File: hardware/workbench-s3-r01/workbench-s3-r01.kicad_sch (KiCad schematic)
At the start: 47 parts, among them J1 YD P1 / RIGHT SOCKET / 1x22, J2 DISPLAY HARNESS / 3V3, J4 EXPANSION / 3V3 IO, J5 EXTERNAL BOOT / GPIO0 TO GND, J6 EXTERNAL RESET / EN TO GND, J7 YD P2 / LEFT SOCKET / 1x22, SW1 KEY_1 MX HOTSWAP, SW10 KEY_10 MX HOTSWAP, SW11 KEY_11 MX HOTSWAP, SW12 KEY_12 MX HOTSWAP, SW13 KEY_13 MX HOTSWAP, SW14 KEY_14 MX HOTSWAP, SW15 KEY_15 MX HOTSWAP, SW16 KEY_16 MX HOTSWAP, SW17 KEY_17 MX HOTSWAP, SW18 KEY_18 MX HOTSWAP, SW2 KEY_2 MX HOTSWAP, SW3 KEY_3 MX HOTSWAP, SW4 KEY_4 MX HOTSWAP, SW5 KEY_5 MX HOTSWAP, SW6 KEY_6 MX HOTSWAP, SW7 KEY_7 MX HOTSWAP, SW8 KEY_8 MX HOTSWAP, SW9 KEY_9 MX HOTSWAP

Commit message: Update application workflows and supporting components
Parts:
- added J8: LOWER / IDC20 TO J9 / 1:1, Connector_IDC:IDC-Header_2x10_P2.54mm_Vertical, symbol Connector_Generic:Conn_02x10_Odd_Even
- added J9: UPPER / IDC20 TO J8 / 1:1, Connector_IDC:IDC-Header_2x10_P2.54mm_Vertical, symbol Connector_Generic:Conn_02x10_Odd_Even
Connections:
- net +3V3: now also J8.2 (Pin_2), J8.20 (Pin_20); no longer C1.1, C2.1, J2.2 (Pin_2), R1.1, R2.1
- net GND: now also J8.1 (Pin_1), J8.12 (Pin_12); no longer C1.2, C2.2, J2.1 (Pin_1)
- net GPIO10: now also J8.9 (Pin_9); no longer SW10.1, SW16.1, SW4.1
- net GPIO11: now also J8.10 (Pin_10); no longer SW11.1, SW17.1, SW5.1
- net GPIO12: now also J8.11 (Pin_11); no longer SW12.1, SW18.1, SW6.1
- net GPIO13: now also J8.13 (Pin_13); no longer J2.4 (Pin_4), R1.2
- net GPIO14: now also J8.14 (Pin_14); no longer J2.3 (Pin_3), R2.2
- net GPIO15: now also J8.15 (Pin_15); no longer J2.5 (Pin_5)
- net GPIO16: now also J8.16 (Pin_16); no longer J2.6 (Pin_6)
- net GPIO17: now also J8.17 (Pin_17); no longer J2.7 (Pin_7)
- net GPIO18: now also J8.18 (Pin_18); no longer J2.8 (Pin_8)
- net GPIO21: now also J8.19 (Pin_19); no longer J2.9 (Pin_9)
- net GPIO4: now also J8.3 (Pin_3); no longer D1.1 (K), D2.1 (K), D3.1 (K), D4.1 (K), D5.1 (K), D6.1 (K)
- net GPIO5: now also J8.4 (Pin_4); no longer D10.1 (K), D11.1 (K), D12.1 (K), D7.1 (K), D8.1 (K), D9.1 (K)
- net GPIO6: now also J8.5 (Pin_5); no longer D13.1 (K), D14.1 (K), D15.1 (K), D16.1 (K), D17.1 (K), D18.1 (K)
- net GPIO7: now also J8.6 (Pin_6); no longer SW1.1, SW13.1, SW7.1
- net GPIO8: now also J8.7 (Pin_7); no longer SW14.1, SW2.1, SW8.1
- net GPIO9: now also J8.8 (Pin_8); no longer SW15.1, SW3.1, SW9.1
- net KEY_10_A renamed UP_KEY_10_A
- net KEY_11_A renamed UP_KEY_11_A
- net KEY_12_A renamed UP_KEY_12_A
- net KEY_13_A renamed UP_KEY_13_A
- net KEY_14_A renamed UP_KEY_14_A
- net KEY_15_A renamed UP_KEY_15_A
- net KEY_16_A renamed UP_KEY_16_A
- net KEY_17_A renamed UP_KEY_17_A
- net KEY_18_A renamed UP_KEY_18_A
- net KEY_1_A renamed UP_KEY_1_A
- net KEY_2_A renamed UP_KEY_2_A
- net KEY_3_A renamed UP_KEY_3_A
- net KEY_4_A renamed UP_KEY_4_A
- net KEY_5_A renamed UP_KEY_5_A
- net KEY_6_A renamed UP_KEY_6_A
- net KEY_7_A renamed UP_KEY_7_A
- net KEY_8_A renamed UP_KEY_8_A
- net KEY_9_A renamed UP_KEY_9_A
- new net UP_3V3: C1.1, C2.1, J2.2 (Pin_2), J9.2 (Pin_2), J9.20 (Pin_20), R1.1, R2.1
- new net UP_GND: C1.2, C2.2, J2.1 (Pin_1), J9.1 (Pin_1), J9.12 (Pin_12)
- new net UP_GPIO10: J9.9 (Pin_9), SW10.1, SW16.1, SW4.1
- new net UP_GPIO11: J9.10 (Pin_10), SW11.1, SW17.1, SW5.1
- new net UP_GPIO12: J9.11 (Pin_11), SW12.1, SW18.1, SW6.1
- new net UP_GPIO13: J2.4 (Pin_4), J9.13 (Pin_13), R1.2
- new net UP_GPIO14: J2.3 (Pin_3), J9.14 (Pin_14), R2.2
- new net UP_GPIO15: J2.5 (Pin_5), J9.15 (Pin_15)
- new net UP_GPIO16: J2.6 (Pin_6), J9.16 (Pin_16)
- new net UP_GPIO17: J2.7 (Pin_7), J9.17 (Pin_17)
- new net UP_GPIO18: J2.8 (Pin_8), J9.18 (Pin_18)
- new net UP_GPIO21: J2.9 (Pin_9), J9.19 (Pin_19)
- new net UP_GPIO4: D1.1 (K), D2.1 (K), D3.1 (K), D4.1 (K), D5.1 (K), D6.1 (K), J9.3 (Pin_3)
- new net UP_GPIO5: D10.1 (K), D11.1 (K), D12.1 (K), D7.1 (K), D8.1 (K), D9.1 (K), J9.4 (Pin_4)
- new net UP_GPIO6: D13.1 (K), D14.1 (K), D15.1 (K), D16.1 (K), D17.1 (K), D18.1 (K), J9.5 (Pin_5)
- new net UP_GPIO7: J9.6 (Pin_6), SW1.1, SW13.1, SW7.1
- new net UP_GPIO8: J9.7 (Pin_7), SW14.1, SW2.1, SW8.1
- new net UP_GPIO9: J9.8 (Pin_8), SW15.1, SW3.1, SW9.1
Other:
- note added: "TWO-BOARD REVIEW DRAFT: J8 to J9 uses a pin-1-to-pin-1 IDC20 cable. NO COPPER ACROSS BREAKAWAY TABS."
- note added: "UP_* nets are on the upper board. Lower and upper nets join ONLY through the external cable; see interconnect.csv."
- note removed: "REVIEW DRAFT: PCB placement only; no routing or fabrication release."
- note removed: "YD ESP32-S3 SOCKETED CARRIER. Reuse native USB-C. Firmware display + diode-matrix rollover support pending."

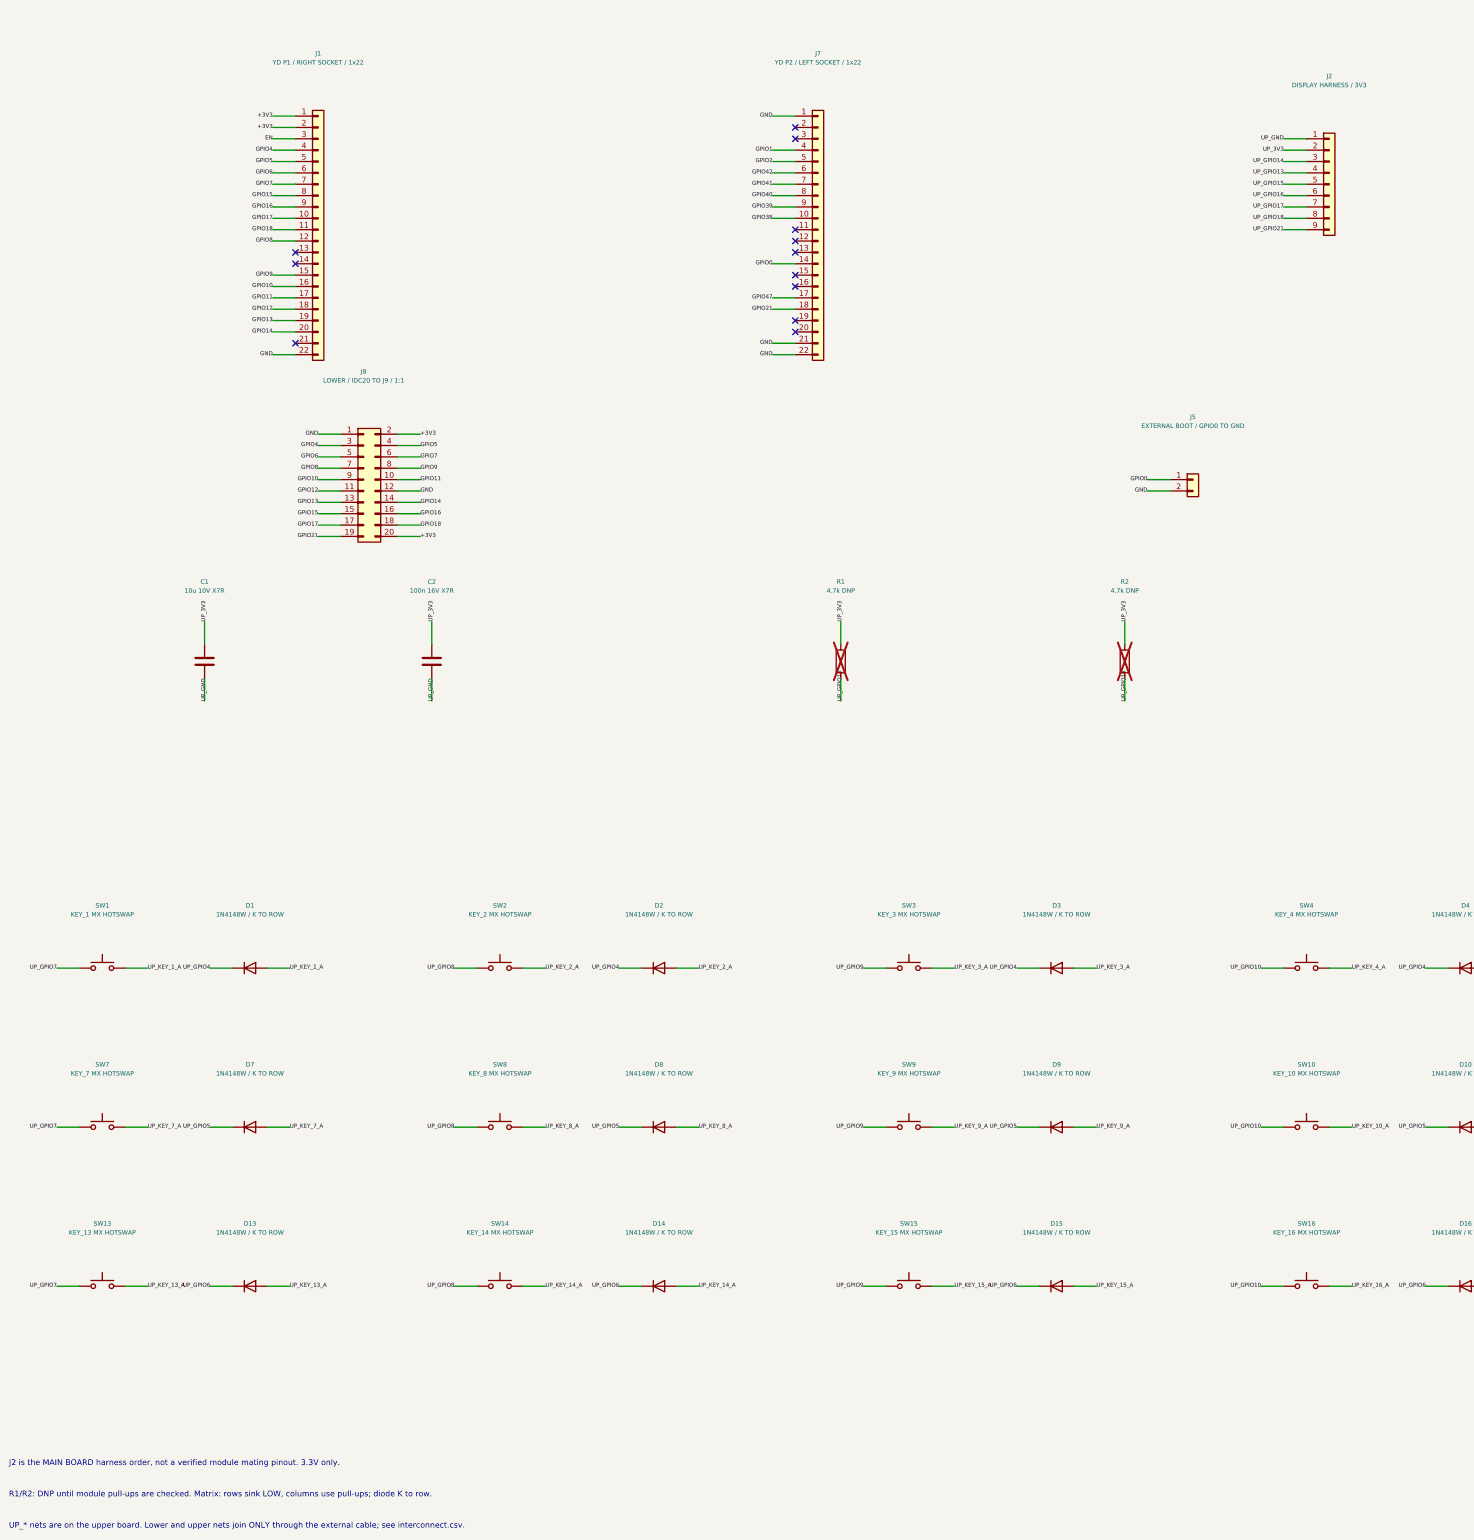
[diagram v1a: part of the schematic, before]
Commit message: fix: correct Workbench S3 display connector and mounting geometry
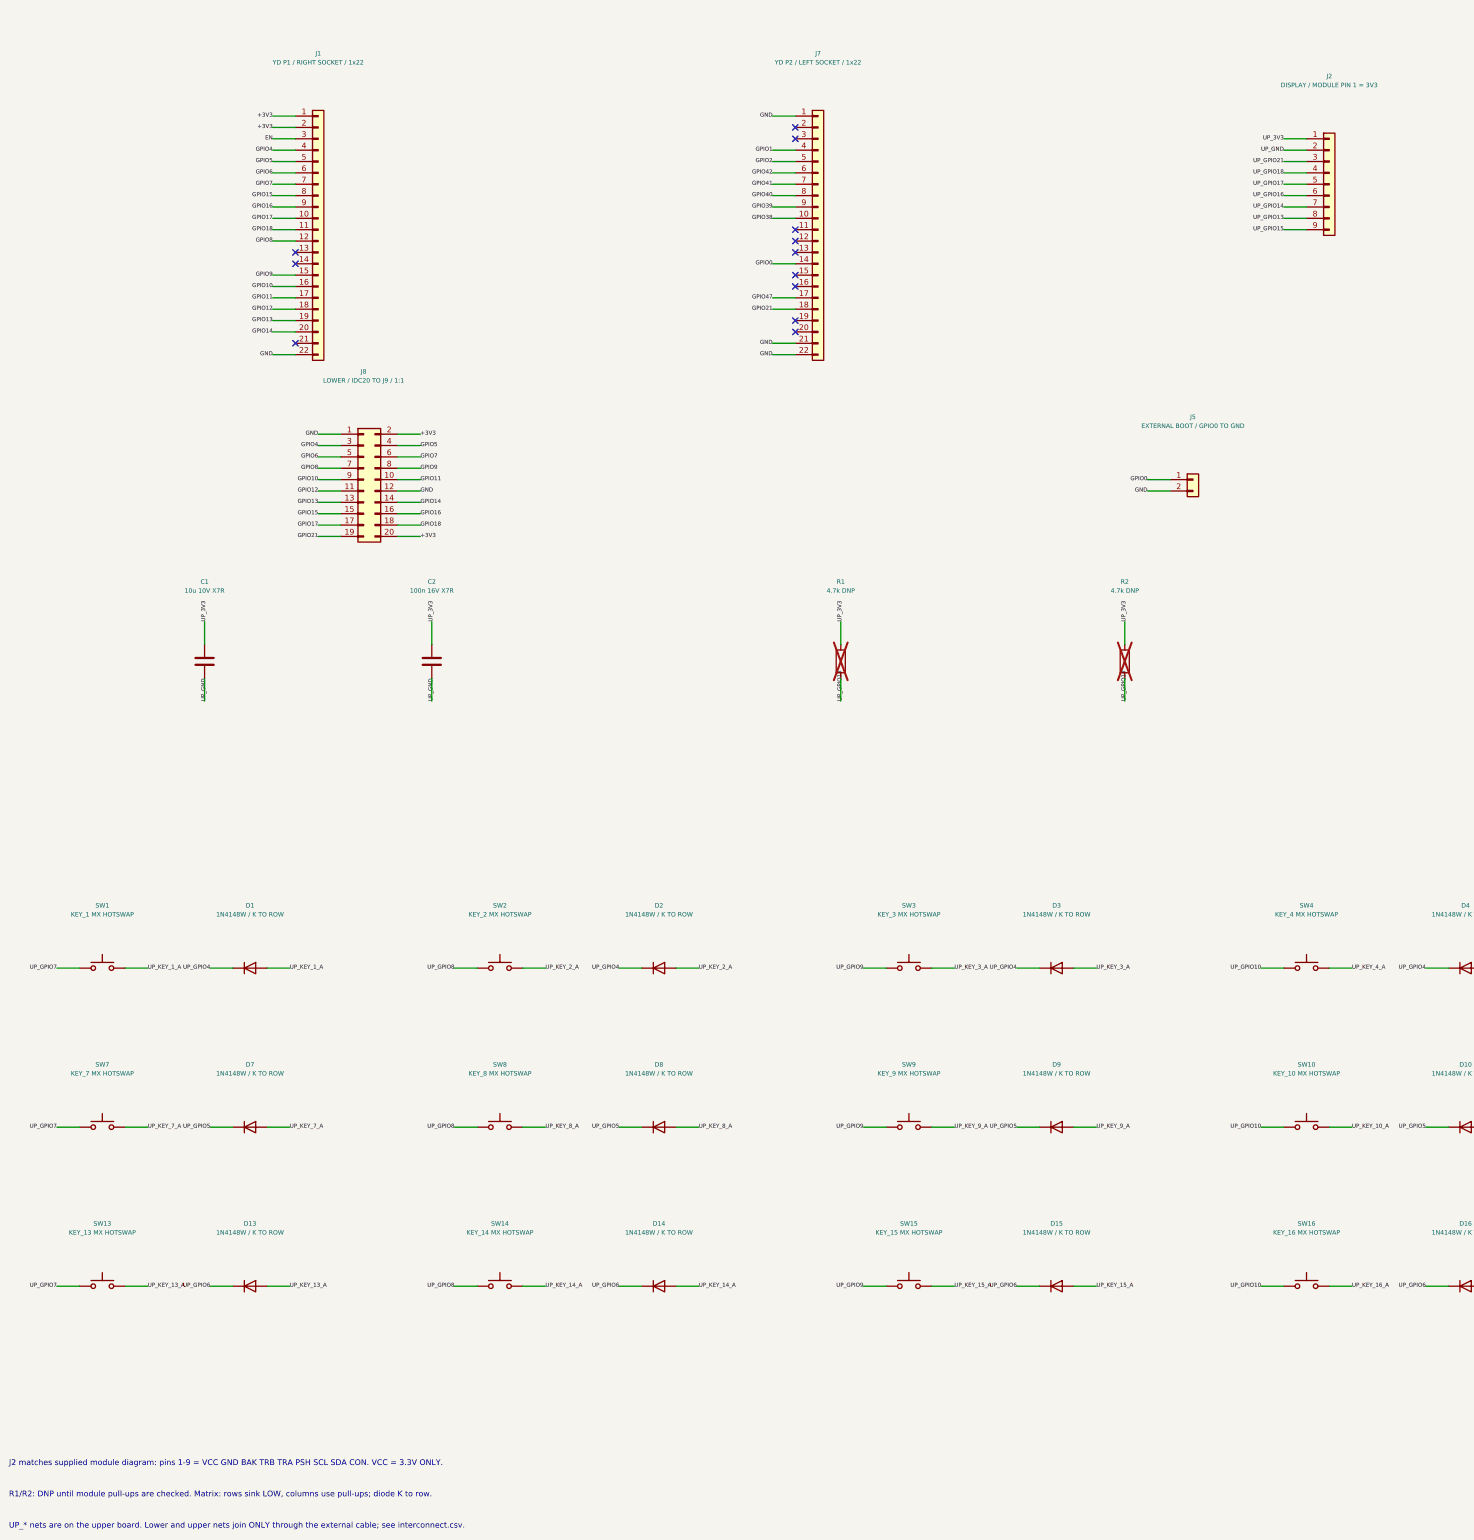
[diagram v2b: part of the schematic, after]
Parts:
- J2: value DISPLAY HARNESS / 3V3 -> DISPLAY / MODULE PIN 1 = 3V3
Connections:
- net UP_3V3: now also J2.1 (Pin_1); no longer J2.2 (Pin_2)
- net UP_GND: now also J2.2 (Pin_2); no longer J2.1 (Pin_1)
- net UP_GPIO13: now also J2.8 (Pin_8); no longer J2.4 (Pin_4)
- net UP_GPIO14: now also J2.7 (Pin_7); no longer J2.3 (Pin_3)
- net UP_GPIO15: now also J2.9 (Pin_9); no longer J2.5 (Pin_5)
- net UP_GPIO17: now also J2.5 (Pin_5); no longer J2.7 (Pin_7)
- net UP_GPIO18: now also J2.4 (Pin_4); no longer J2.8 (Pin_8)
- net UP_GPIO21: now also J2.3 (Pin_3); no longer J2.9 (Pin_9)
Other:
- note added: "J2 matches supplied module diagram: pins 1-9 = VCC GND BAK TRB TRA PSH SCL SDA CON. VCC = 3.3V ONLY."
- note removed: "J2 is the MAIN BOARD harness order, not a verified module mating pinout. 3.3V only."
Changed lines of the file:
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@@
       )
     )
-    (property "Value" "DISPLAY HARNESS / 3V3"
+    (property "Value" "DISPLAY / MODULE PIN 1 = 3V3"
       (at 330.2 71.82000000000001 0)
       (effects
@@
     )
   )
-  (label "UP_GND"
+  (label "UP_3V3"
     (at 320.04 83.82 0)
     (effects
@@
     )
   )
-  (label "UP_3V3"
+  (label "UP_GND"
     (at 320.04 86.36 0)
     (effects
@@
     )
   )
-  (label "UP_GPIO14"
+  (label "UP_GPIO21"
     (at 320.04 88.9 0)
     (effects
@@
     )
   )
-  (label "UP_GPIO13"
+  (label "UP_GPIO18"
     (at 320.04 91.44 0)
     (effects
@@
     )
   )
-  (label "UP_GPIO15"
+  (label "UP_GPIO17"
     (at 320.04 93.98 0)
     (effects
@@
     )
   )
-  (label "UP_GPIO17"
+  (label "UP_GPIO14"
     (at 320.04 99.06 0)
     (effects
@@
     )
   )
-  (label "UP_GPIO18"
+  (label "UP_GPIO13"
     (at 320.04 101.6 0)
     (effects
@@
     )
   )
-  (label "UP_GPIO21"
+  (label "UP_GPIO15"
     (at 320.04 104.14 0)
     (effects
@@
     )
   )
-  (text "J2 is the MAIN BOARD harness order, not a verified module mating pinout. 3.3V only."
+  (text "J2 matches supplied module diagram: pins 1-9 = VCC GND BAK TRB TRA PSH SCL SDA CON. VCC = 3.3V ONLY."
     (at 35 380 0)
     (effects

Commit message: Update application implementation and supporting files
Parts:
- added C3: 100n 16V X7R / U1, Capacitor_SMD:C_0805_2012Metric_Pad1.18x1.45mm_HandSolder, symbol Device:C
- added R4: 10k U1 RESET PULLUP, Resistor_SMD:R_0805_2012Metric_Pad1.20x1.40mm_HandSolder, symbol Device:R
- added U1: MCP23017-E/SO / 0x20, Package_SO:SOIC-28W_7.5x17.9mm_P1.27mm, symbol Interface_Expansion:MCP23017x-x-SO
- J4: value EXPANSION / 3V3 IO -> EXPANSION / 22 SPARE GPIO / 3V3 IO; footprint Connector_PinHeader_2.54mm:PinHeader_1x10_P2.54mm_Vertical -> Connector_PinHeader_2.54mm:PinHeader_1x24_P2.54mm_Vertical; symbol Connector_Generic:Conn_01x10 -> Connector_Generic:Conn_01x24
- J8: value LOWER / IDC20 TO J9 / 1:1 -> LOWER / I2C4 TO J9 / 1:1; footprint Connector_IDC:IDC-Header_2x10_P2.54mm_Vertical -> Connector_JST:JST_XH_B4B-XH-A_1x04_P2.50mm_Vertical; symbol Connector_Generic:Conn_02x10_Odd_Even -> Connector_Generic:Conn_01x04
- J9: value UPPER / IDC20 TO J8 / 1:1 -> UPPER / I2C4 TO J8 / 1:1; footprint Connector_IDC:IDC-Header_2x10_P2.54mm_Vertical -> Connector_JST:JST_XH_B4B-XH-A_1x04_P2.50mm_Vertical; symbol Connector_Generic:Conn_02x10_Odd_Even -> Connector_Generic:Conn_01x04
- R1, R2: value 4.7k DNP -> 2.2k I2C PULLUP; now fitted
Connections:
- net +3V3: no longer J8.20 (Pin_20)
- net GND: no longer J8.12 (Pin_12)
- net GPIO10: now also J4.11 (Pin_11); no longer J8.9 (Pin_9)
- net GPIO11: now also J4.12 (Pin_12); no longer J8.10 (Pin_10)
- net GPIO12: now also J4.13 (Pin_13); no longer J8.11 (Pin_11)
- net GPIO13: now also J8.3 (Pin_3); no longer J8.13 (Pin_13)
- net GPIO14: now also J8.4 (Pin_4); no longer J8.14 (Pin_14)
- net GPIO15: now also J4.14 (Pin_14); no longer J8.15 (Pin_15)
- net GPIO16: now also J4.15 (Pin_15); no longer J8.16 (Pin_16)
- net GPIO17: now also J4.16 (Pin_16); no longer J8.17 (Pin_17)
- net GPIO18: now also J4.17 (Pin_17); no longer J8.18 (Pin_18)
- net GPIO21: now also J4.18 (Pin_18); no longer J8.19 (Pin_19)
- net GPIO38: now also J4.19 (Pin_19); no longer J4.5 (Pin_5)
- net GPIO39: now also J4.20 (Pin_20); no longer J4.6 (Pin_6)
- net GPIO4: now also J4.5 (Pin_5); no longer J8.3 (Pin_3)
- net GPIO40: now also J4.21 (Pin_21); no longer J4.7 (Pin_7)
- net GPIO41: now also J4.22 (Pin_22); no longer J4.8 (Pin_8)
- net GPIO42: now also J4.23 (Pin_23); no longer J4.9 (Pin_9)
- net GPIO47: now also J4.24 (Pin_24); no longer J4.10 (Pin_10)
- net GPIO5: now also J4.6 (Pin_6); no longer J8.4 (Pin_4)
- net GPIO6: now also J4.7 (Pin_7); no longer J8.5 (Pin_5)
- net GPIO7: now also J4.8 (Pin_8); no longer J8.6 (Pin_6)
- net GPIO8: now also J4.9 (Pin_9); no longer J8.7 (Pin_7)
- net GPIO9: now also J4.10 (Pin_10); no longer J8.8 (Pin_8)
- net UP_3V3: now also C3.1, R4.1, U1.9 (V_{DD}); no longer J9.20 (Pin_20)
- net UP_GND: now also C3.2, U1.10 (V_{SS}), U1.15 (A0), U1.16 (A1), U1.17 (A2); no longer J9.12 (Pin_12)
- net UP_GPIO13: now also J9.3 (Pin_3), U1.13 (SDA); no longer J9.13 (Pin_13)
- net UP_GPIO14: now also J9.4 (Pin_4), U1.12 (SCK); no longer J9.14 (Pin_14)
- net UP_GPIO10 renamed UP_GPB3
- net UP_GPB3: now also U1.4 (GPB3); no longer J9.9 (Pin_9)
- net UP_GPIO11 renamed UP_GPB4
- net UP_GPB4: now also U1.5 (GPB4); no longer J9.10 (Pin_10)
- net UP_GPIO12 renamed UP_GPB5
- net UP_GPB5: now also U1.6 (GPB5); no longer J9.11 (Pin_11)
- net UP_GPIO15 renamed UP_GPA0
- net UP_GPA0: now also U1.21 (GPA0); no longer J9.15 (Pin_15)
- net UP_GPIO16 renamed UP_GPA1
- net UP_GPA1: now also U1.22 (GPA1); no longer J9.16 (Pin_16)
- net UP_GPIO17 renamed UP_GPA2
- net UP_GPA2: now also U1.23 (GPA2); no longer J9.17 (Pin_17)
- net UP_GPIO18 renamed UP_GPA3
- net UP_GPA3: now also U1.24 (GPA3); no longer J9.18 (Pin_18)
- net UP_GPIO21 renamed UP_GPA4
- net UP_GPA4: now also U1.25 (GPA4); no longer J9.19 (Pin_19)
- net UP_GPIO4 renamed UP_GPA5
- net UP_GPA5: now also U1.26 (GPA5); no longer J9.3 (Pin_3)
- net UP_GPIO5 renamed UP_GPA6
- net UP_GPA6: now also U1.27 (GPA6); no longer J9.4 (Pin_4)
- net UP_GPIO6 renamed UP_GPA7
- net UP_GPA7: now also U1.28 (GPA7); no longer J9.5 (Pin_5)
- net UP_GPIO7 renamed UP_GPB0
- net UP_GPB0: now also U1.1 (GPB0); no longer J9.6 (Pin_6)
- net UP_GPIO8 renamed UP_GPB1
- net UP_GPB1: now also U1.2 (GPB1); no longer J9.7 (Pin_7)
- net UP_GPIO9 renamed UP_GPB2
- net UP_GPB2: now also U1.3 (GPB2); no longer J9.8 (Pin_8)
- new net UP_IO_RESET: R4.2, U1.18 (~{RESET})
- no-connect marks 12 -> 18
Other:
- note added: "I2C4 TWO-BOARD DRAFT: J8/J9 pins 1-4 = GND 3V3 SDA SCL. MCP23017 at 0x20 shares the OLED bus."
- note added: "R1/R2: 2.2k I2C pull-ups; check module parallel pull-ups. GPA5-7 rows: selected LOW, inactive HIGH; diode K to row."
- note removed: "R1/R2: DNP until module pull-ups are checked. Matrix: rows sink LOW, columns use pull-ups; diode K to row."
- note removed: "TWO-BOARD REVIEW DRAFT: J8 to J9 uses a pin-1-to-pin-1 IDC20 cable. NO COPPER ACROSS BREAKAWAY TABS."
